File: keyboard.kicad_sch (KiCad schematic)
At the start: 8 parts, among them SW1 SW_Push, SW2 SW_Push, SW3 SW_Push, SW4 SW_Push, SW5 SW_Push, SW6 SW_Push

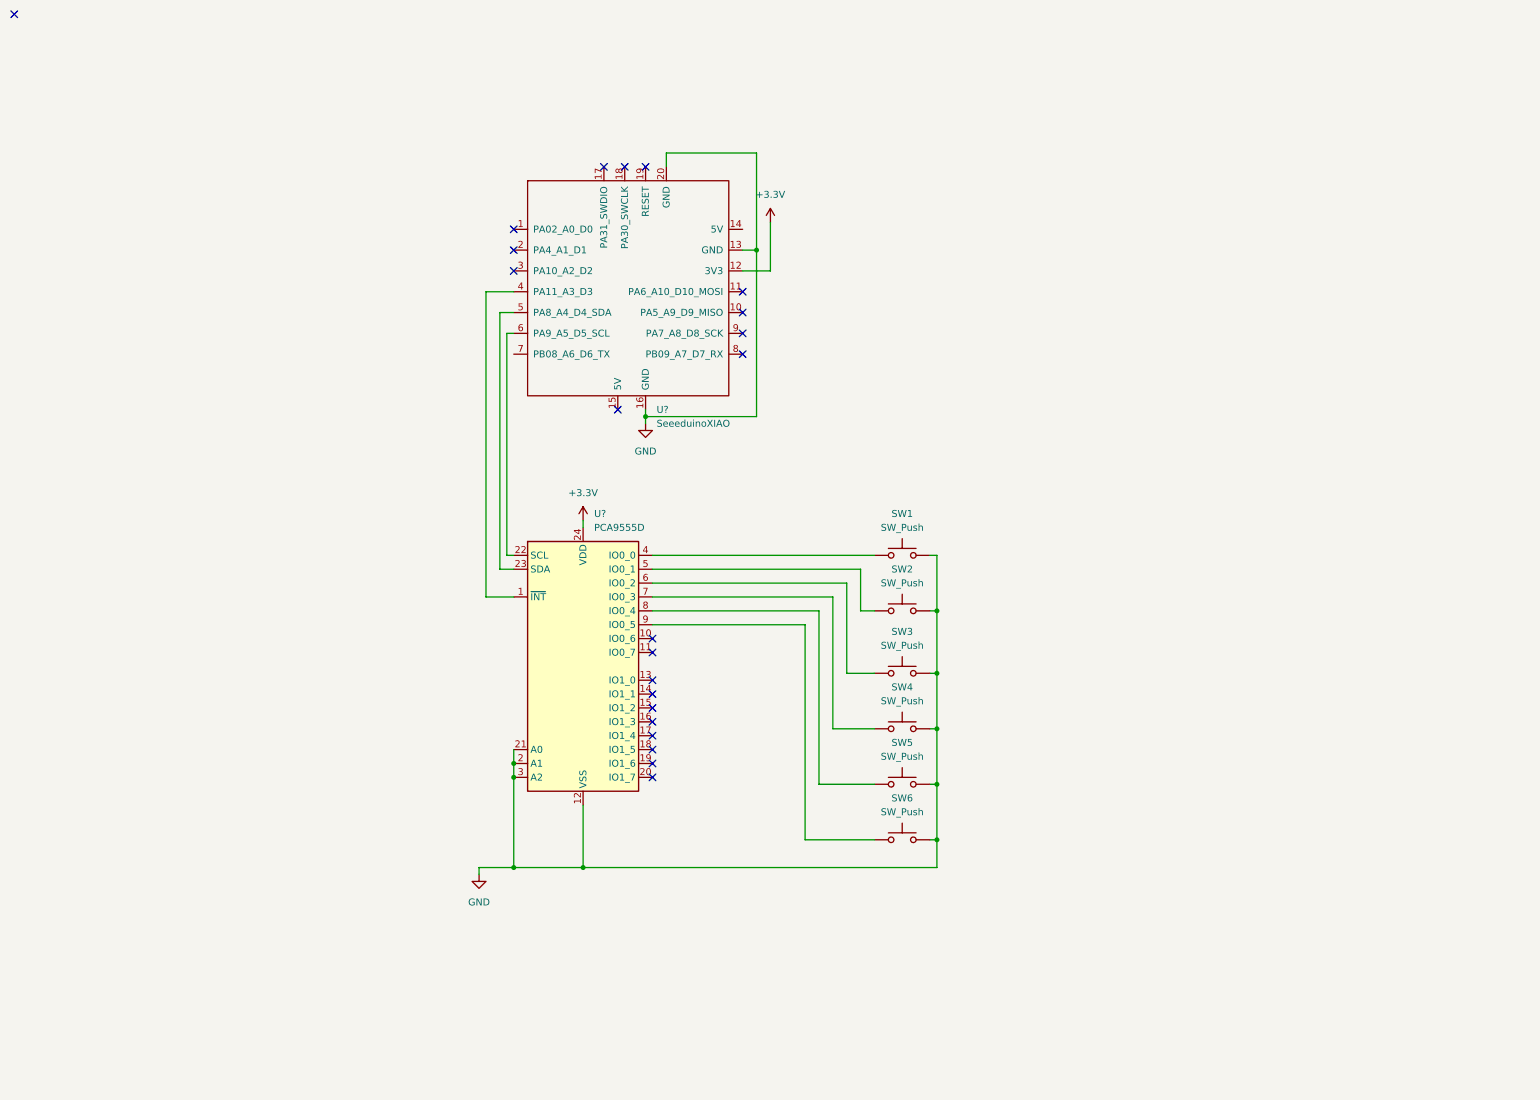
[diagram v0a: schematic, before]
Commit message: Finished basic keyboard design based on seeduino
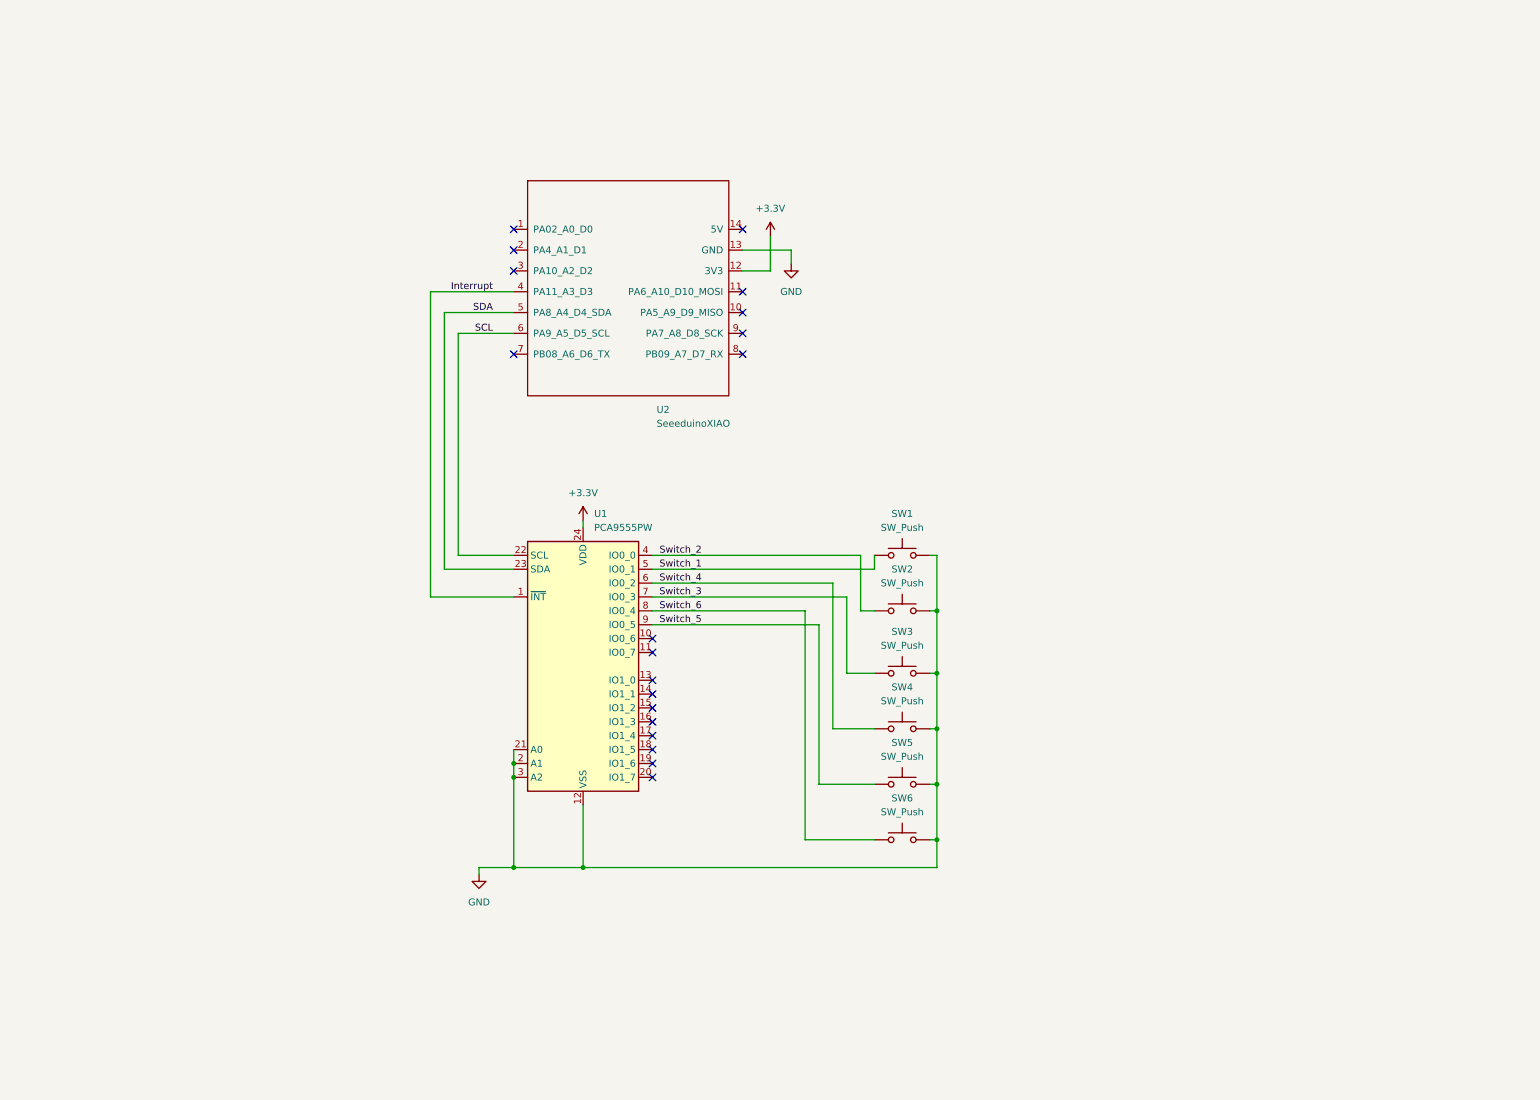
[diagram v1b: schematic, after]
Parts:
- U1: renamed from U?; value PCA9555D -> PCA9555PW; footprint Package_SO:SOIC-24W_7.5x15.4mm_P1.27mm -> Package_SO:TSSOP-24_4.4x7.8mm_P0.65mm
- gave numbers to parts that had none: 1
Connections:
- net GND: no longer U2.16 (GND), U2.20 (GND)
- net Switch_1: now reaches U1.5 (IO0_1)
- net Switch_1: now also SW1.1; no longer SW2.1
- net Switch_3: now reaches U1.7 (IO0_3)
- net Switch_3: now also SW3.1; no longer SW4.1
- net Switch_4: now reaches U1.6 (IO0_2)
- net Switch_4: now also SW4.1; no longer SW3.1
- net Switch_5: now reaches U1.9 (IO0_5)
- net Switch_5: now also SW5.1; no longer SW6.1
- net Switch_2: now reaches U1.4 (IO0_0)
- net Switch_2: now also SW2.1; no longer SW1.1
- net Interrupt: now reaches U1.1 (~{INT}), U2.4 (PA11_A3_D3)
- net SCL: now reaches U1.22 (SCL), U2.6 (PA9_A5_D5_SCL)
- net SDA: now reaches U1.23 (SDA), U2.5 (PA8_A4_D4_SDA)
- net Switch_6: now reaches U1.8 (IO0_4)
- net Switch_6: now also SW6.1; no longer SW5.1
- no-connect marks 22 -> 19

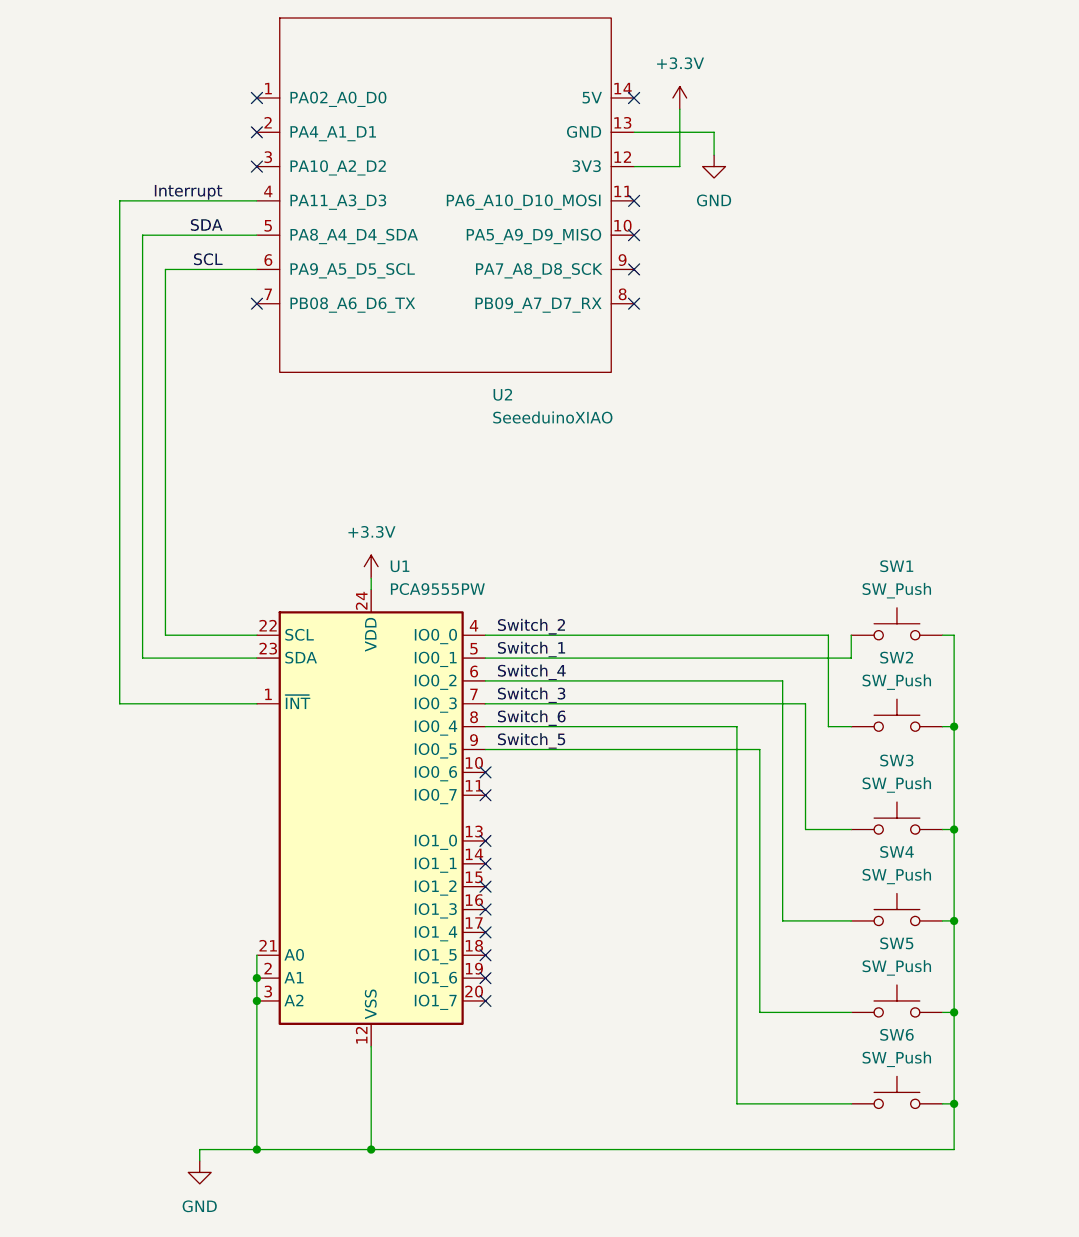
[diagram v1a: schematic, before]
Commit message: Moved to new switch footprint library
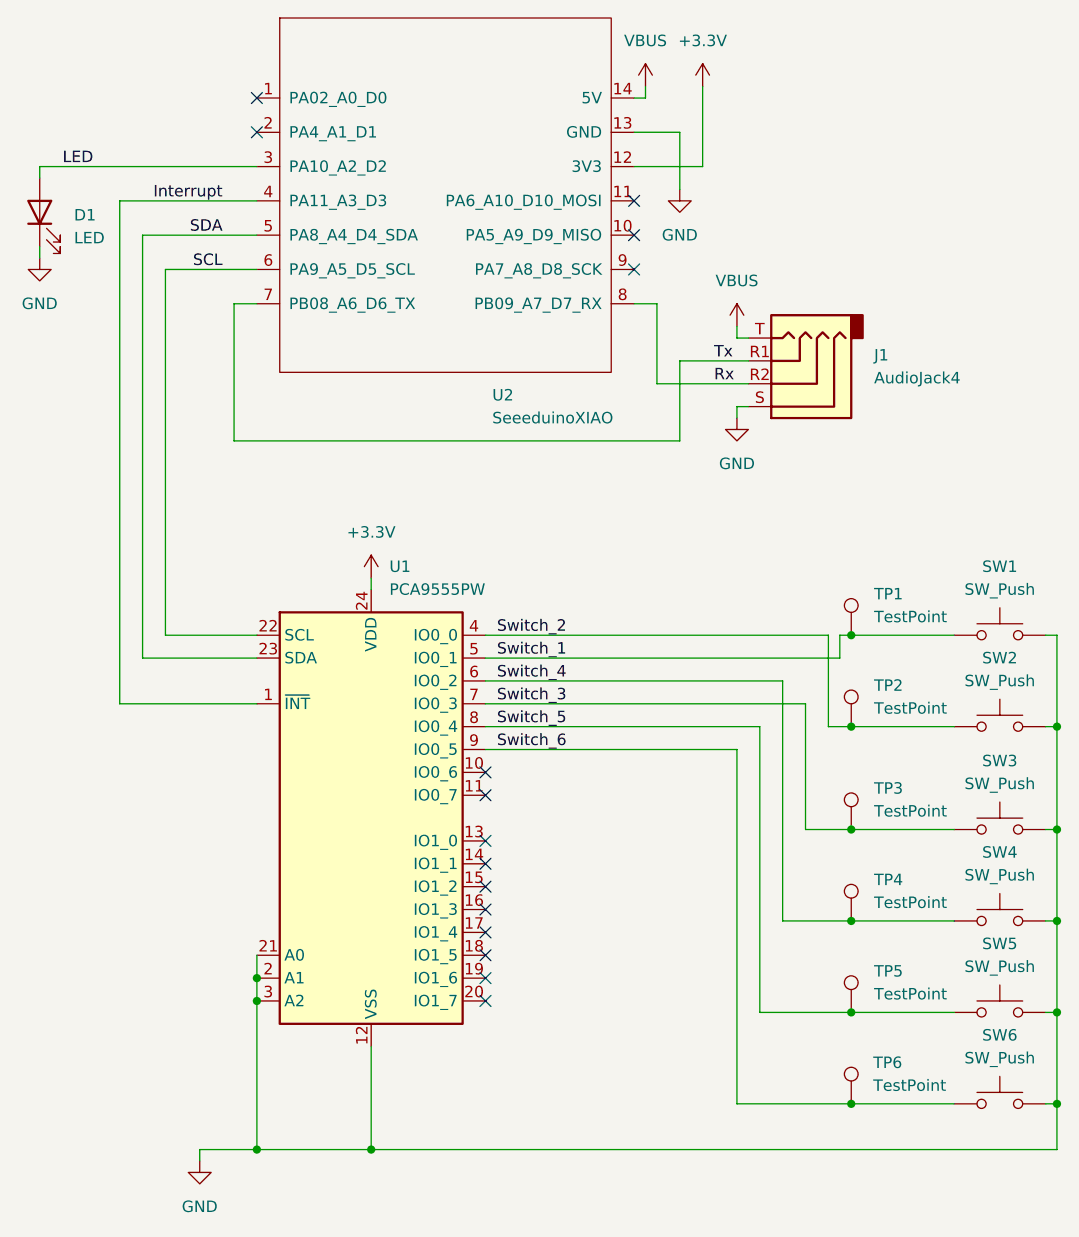
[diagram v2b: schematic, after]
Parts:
- added D1: LED, LED_SMD:LED_1206_3216Metric_Pad1.42x1.75mm_HandSolder, symbol Device:LED
- added J1: AudioJack4, Connector_Audio:Jack_3.5mm_PJ320D_Horizontal, symbol Connector:AudioJack4
- added TP1, TP2, TP3, TP4, TP5, TP6: TestPoint, TestPoint:TestPoint_Pad_D1.0mm, symbol Connector:TestPoint
- SW1, SW2, SW3, SW4, SW5, SW6: footprint Keyboard Switches:SW_PG1350 -> Switch_Keyboard_Kailh:SW_Kailh_Choc_V1_1.00u
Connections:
- net GND: now also D1.1 (K), J1.S
- net Switch_1: now also TP1.1
- net Switch_2: now also TP2.1
- net Switch_3: now also TP3.1
- net Switch_4: now also TP4.1
- net Switch_5: now also U1.8 (IO0_4), TP5.1; no longer U1.9 (IO0_5)
- net Switch_6: now also U1.9 (IO0_5), TP6.1; no longer U1.8 (IO0_4)
- net VBUS: now reaches U2.14 (5V)
- net VBUS: now also J1.T
- net LED: now reaches U2.3 (PA10_A2_D2)
- net LED: now also D1.2 (A)
- net Tx: now reaches U2.7 (PB08_A6_D6_TX)
- net Tx: now also J1.R1
- net Rx: now reaches U2.8 (PB09_A7_D7_RX)
- net Rx: now also J1.R2
- no-connect marks 19 -> 15
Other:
- moved on the sheet: SW1

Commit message: Finished split keyboard prototype
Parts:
- removed J1: AudioJack4, Connector_Audio:Jack_3.5mm_PJ320D_Horizontal, symbol Connector:AudioJack4
- added D2: LED, LED_SMD:LED_1206_3216Metric_Pad1.42x1.75mm_HandSolder, symbol Device:LED
- added J1, J2: USB_C_Receptacle_USB2.0, Connector_USB:USB_C_Receptacle_GCT_USB4105-xx-A_16P_TopMnt_Horizontal, symbol Connector:USB_C_Receptacle_USB2.0
- added R1, R2: 1k, Resistor_SMD:R_1206_3216Metric_Pad1.30x1.75mm_HandSolder, symbol Device:R
- added SW10, SW11, SW12, SW7, SW8, SW9: SW_Push, Switch_Keyboard_Kailh:SW_Kailh_Choc_Mini_1.00u, symbol Switch:SW_Push
- added TP10, TP11, TP12, TP13, TP14, TP7, TP8, TP9: TestPoint, TestPoint:TestPoint_Pad_D1.0mm, symbol Connector:TestPoint
- added U2: PCA9555PW, Package_SO:TSSOP-24_4.4x7.8mm_P0.65mm, symbol Interface_Expansion:PCA9555D
- renumbered U2 to U3
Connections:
- net GND: now also J1.A1 (GND), J1.A12 (GND), J1.B1 (GND), J1.B12 (GND)
- net +3.3V renamed +3V3
- net +3V3: now also J1.A4 (VBUS), J1.A9 (VBUS), J1.B4 (VBUS), J1.B9 (VBUS)
- net Interrupt renamed Interrupt_L
- net Interrupt_L: now also J1.A5 (CC1), J1.B5 (CC2), TP13.1
- net LED renamed LED_L
- net LED_L: now also R1.1; no longer U3.3 (PA10_A2_D2)
- net Rx: no longer names the net of U3.8 (PB09_A7_D7_RX)
- net SCL renamed SCL_L
- net SCL_L: now also J1.A7 (D-), J1.B7 (D-)
- net SDA renamed SDA_L
- net SDA_L: now also J1.A6 (D+), J1.B6 (D+)
- net Tx: no longer names the net of U3.7 (PB08_A6_D6_TX)
- net VBUS: no longer names the net of U3.14 (5V)
- new net 3V3_R: J2.A4 (VBUS), J2.A9 (VBUS), J2.B4 (VBUS), J2.B9 (VBUS), R2.1, U2.21 (A0), U2.24 (VDD)
- new net GND_R: D2.1 (K), J2.A1 (GND), J2.A12 (GND), J2.B1 (GND), J2.B12 (GND), SW10.1, SW11.1, SW12.1, SW7.1, SW8.1, SW9.1, U2.12 (VSS), U2.2 (A1), U2.3 (A2)
- new net Interrupt_R: J2.A5 (CC1), J2.B5 (CC2), TP14.1, U2.1 (~{INT})
- new net LED_PIN: R1.2, U3.3 (PA10_A2_D2)
- new net LED_R: D2.2 (A), R2.2
- new net SCL_R: J2.A7 (D-), J2.B7 (D-), U2.22 (SCL)
- new net SDA_R: J2.A6 (D+), J2.B6 (D+), U2.23 (SDA)
- new net Switch_10: SW10.2, TP10.1, U2.6 (IO0_2)
- new net Switch_11: SW11.2, TP11.1, U2.4 (IO0_0)
- new net Switch_12: SW12.2, TP12.1, U2.5 (IO0_1)
- new net Switch_7: SW7.2, TP7.1, U2.9 (IO0_5)
- new net Switch_8: SW8.2, TP8.1, U2.8 (IO0_4)
- new net Switch_9: SW9.2, TP9.1, U2.7 (IO0_3)
- no-connect marks 15 -> 34
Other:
- note added: "Left half"
- note added: "Left hand side has the address 000 (MSB->LSB)"
- note added: "Right half"
- note added: "Right hand side has the address 001 (MSB->LSB)"
- moved on the sheet: D1, SW1, SW2, SW3, SW4, SW5, SW6, TP1, TP2, TP3, TP4, TP5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
